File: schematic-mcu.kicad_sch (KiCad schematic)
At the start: 24 parts, among them U5 USBLC6-2P6, U6 ESP32-S3FN8, Y1 Crystal_GND24

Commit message: PCB Drawing
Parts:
- C1, C2, C28, C29, C30, C31, C32, C33, C34, C35, C4, C5, C8: footprint (none) -> Capacitor_SMD:C_1206_3216Metric
- L3: footprint (none) -> Inductor_SMD:LQG15WH0N7B02D
- R23, R5: footprint (none) -> Resistor_SMD:R_1206_3216Metric
- Y1: footprint (none) -> Crystal:KC3225K400000C1GE00
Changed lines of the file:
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@@
       (effects (font (size 1.27 1.27)) (justify left))
     )
-    (property "Footprint" "" (at 186.3852 60.96 0)
+    (property "Footprint" "Capacitor_SMD:C_1206_3216Metric" (at 186.3852 60.96 0)
       (effects (font (size 1.27 1.27)) hide)
     )
@@
       (effects (font (size 1.27 1.27)) (justify left))
     )
-    (property "Footprint" "" (at 164.7952 60.96 0)
+    (property "Footprint" "Capacitor_SMD:C_1206_3216Metric" (at 164.7952 60.96 0)
       (effects (font (size 1.27 1.27)) hide)
     )
@@
       (effects (font (size 1.27 1.27)) (justify left))
     )
-    (property "Footprint" "" (at 176.2252 60.96 0)
+    (property "Footprint" "Capacitor_SMD:C_1206_3216Metric" (at 176.2252 60.96 0)
       (effects (font (size 1.27 1.27)) hide)
     )
@@
       (effects (font (size 1.27 1.27)) (justify left))
     )
-    (property "Footprint" "" (at 213.0552 46.99 0)
+    (property "Footprint" "Capacitor_SMD:C_1206_3216Metric" (at 213.0552 46.99 0)
       (effects (font (size 1.27 1.27)) hide)
     )
@@
       (effects (font (size 1.27 1.27)) (justify left))
     )
-    (property "Footprint" "" (at 83.5152 49.53 0)
+    (property "Footprint" "Capacitor_SMD:C_1206_3216Metric" (at 83.5152 49.53 0)
       (effects (font (size 1.27 1.27)) hide)
     )
@@
       (effects (font (size 1.27 1.27)))
     )
-    (property "Footprint" "" (at 194.31 53.34 0)
+    (property "Footprint" "Inductor_SMD:LQG15WH0N7B02D" (at 194.31 53.34 0)
       (effects (font (size 1.27 1.27)) hide)
     )
@@
       (effects (font (size 1.27 1.27)) (justify left))
     )
-    (property "Footprint" "" (at 124.1552 49.53 0)
+    (property "Footprint" "Capacitor_SMD:C_1206_3216Metric" (at 124.1552 49.53 0)
       (effects (font (size 1.27 1.27)) hide)
     )
@@
       (effects (font (size 1.27 1.27)) (justify right))
     )
-    (property "Footprint" "" (at 124.968 36.83 90)
+    (property "Footprint" "Resistor_SMD:R_1206_3216Metric" (at 124.968 36.83 90)
       (effects (font (size 1.27 1.27)) hide)
     )
@@
       (effects (font (size 1.27 1.27)) hide)
     )
-    (property "Footprint" "" (at 45.72 162.56 0)
+    (property "Footprint" "Crystal:KC3225K400000C1GE00" (at 45.72 162.56 0)
       (effects (font (size 1.27 1.27)) hide)
     )
@@
       (effects (font (size 1.27 1.27)) (justify left))
     )
-    (property "Footprint" "" (at 74.6252 114.3 0)
+    (property "Footprint" "Capacitor_SMD:C_1206_3216Metric" (at 74.6252 114.3 0)
       (effects (font (size 1.27 1.27)) hide)
     )
@@
       (effects (font (size 1.27 1.27)) (justify right))
     )
-    (property "Footprint" "" (at 44.958 36.83 90)
+    (property "Footprint" "Resistor_SMD:R_1206_3216Metric" (at 44.958 36.83 90)
       (effects (font (size 1.27 1.27)) hide)
     )
@@
       (effects (font (size 1.27 1.27)) (justify left))
     )
-    (property "Footprint" "" (at 257.5052 63.5 0)
+    (property "Footprint" "Capacitor_SMD:C_1206_3216Metric" (at 257.5052 63.5 0)
       (effects (font (size 1.27 1.27)) hide)
     )
@@
       (effects (font (size 1.27 1.27)) (justify left))
     )
-    (property "Footprint" "" (at 33.9852 172.72 0)
+    (property "Footprint" "Capacitor_SMD:C_1206_3216Metric" (at 33.9852 172.72 0)
       (effects (font (size 1.27 1.27)) hide)
     )
@@
       (effects (font (size 1.27 1.27)) (justify right))
     )
-    (property "Footprint" "" (at 245.4148 63.5 0)
+    (property "Footprint" "Capacitor_SMD:C_1206_3216Metric" (at 245.4148 63.5 0)
       (effects (font (size 1.27 1.27)) hide)
     )
@@
       (effects (font (size 1.27 1.27)) (justify right))
     )
-    (property "Footprint" "" (at 84.328 36.83 90)
+    (property "Footprint" "Resistor_SMD:R_1206_3216Metric" (at 84.328 36.83 90)
       (effects (font (size 1.27 1.27)) hide)
     )
@@
       (effects (font (size 1.27 1.27)) (justify left))
     )
-    (property "Footprint" "" (at 243.5352 46.99 0)
+    (property "Footprint" "Capacitor_SMD:C_1206_3216Metric" (at 243.5352 46.99 0)
       (effects (font (size 1.27 1.27)) hide)
     )
@@
       (effects (font (size 1.27 1.27)) hide)
     )
-    (property "Value" "PWR_FLAG" (at 219.71 48.26 0)
+    (property "Value" "PWR_FLAG" (at 219.71 49.53 0)
       (effects (font (size 1.27 1.27)))
     )
@@
       (effects (font (size 1.27 1.27)) (justify left))
     )
-    (property "Footprint" "" (at 204.1652 60.96 0)
+    (property "Footprint" "Capacitor_SMD:C_1206_3216Metric" (at 204.1652 60.96 0)
       (effects (font (size 1.27 1.27)) hide)
     )
@@
       (effects (font (size 1.27 1.27)) (justify left))
     )
-    (property "Footprint" "" (at 44.1452 49.53 0)
+    (property "Footprint" "Capacitor_SMD:C_1206_3216Metric" (at 44.1452 49.53 0)
       (effects (font (size 1.27 1.27)) hide)
     )
@@
       (effects (font (size 1.27 1.27)) (justify left))
     )
-    (property "Footprint" "" (at 58.1152 172.72 0)
-      (effects (font (size 1.27 1.27)) hide)
-    )
+    (property "Footprint" "Capacitor_SMD:C_1206_3216Metric" (at 58.1152 172.72 0)
+      (effects (font (size 1.27 1.27)) hide)
+    )

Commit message: Changing footprints for capacitors C >= 10 uF
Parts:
- C32: footprint Capacitor_SMD:C_1206_3216Metric -> Capacitor_Tantalum_SMD:EEHZT1E331UP
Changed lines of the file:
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@@
       (effects (font (size 1.27 1.27)) (justify left))
     )
-    (property "Footprint" "Capacitor_SMD:C_1206_3216Metric" (at 164.7952 60.96 0)
+    (property "Footprint" "Capacitor_Tantalum_SMD:EEHZT1E331UP" (at 164.7952 60.96 0)
       (effects (font (size 1.27 1.27)) hide)
     )

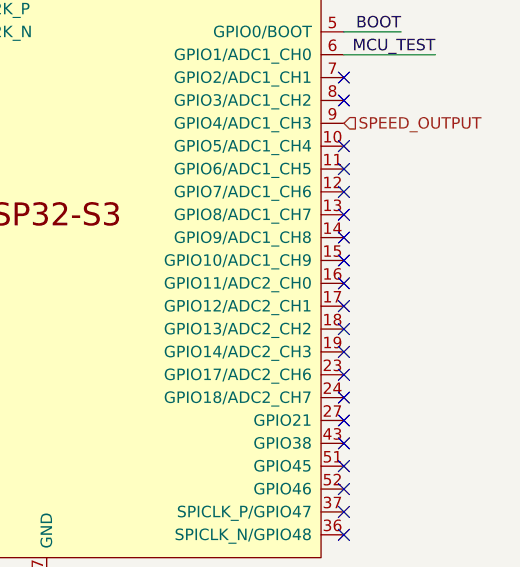
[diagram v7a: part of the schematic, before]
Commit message: Add test pins for I/O MCU
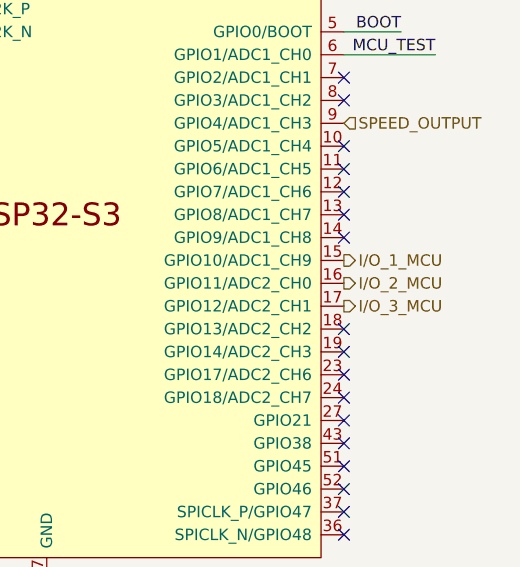
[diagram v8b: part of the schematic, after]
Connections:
- net I/O_1_MCU: now reaches U6.15 (GPIO10/ADC1_CH9)
- net I/O_2_MCU: now reaches U6.16 (GPIO11/ADC2_CH0)
- net I/O_3_MCU: now reaches U6.17 (GPIO12/ADC2_CH1)
- no-connect marks 36 -> 33
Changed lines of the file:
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@@
   (no_connect (at 195.58 128.27))
   (no_connect (at 195.58 138.43))
-  (no_connect (at 261.62 95.25))
-  (no_connect (at 261.62 118.11))
   (no_connect (at 261.62 107.95))
   (no_connect (at 261.62 113.03))
   (no_connect (at 195.58 87.63))
-  (no_connect (at 261.62 120.65))
   (no_connect (at 195.58 146.05))
   (no_connect (at 261.62 140.97))
@@
   (no_connect (at 195.58 140.97))
   (no_connect (at 261.62 74.93))
-  (no_connect (at 261.62 97.79))
   (no_connect (at 261.62 128.27))
   (no_connect (at 261.62 123.19))
   (no_connect (at 261.62 133.35))
   (no_connect (at 261.62 138.43))
-  (no_connect (at 261.62 115.57))
+  (no_connect (at 261.62 95.25))
   (no_connect (at 261.62 146.05))
   (no_connect (at 261.62 110.49))
@@
   (no_connect (at 195.58 110.49))
   (no_connect (at 261.62 135.89))
+  (no_connect (at 261.62 97.79))
   (no_connect (at 261.62 105.41))
   (wire (pts (xy 163.83 62.23) (xy 163.83 60.96))
@@
     (effects (font (size 1.27 1.27)) (justify right))
   )
+  (hierarchical_label "I{slash}O_3_MCU" (shape output) (at 261.62 120.65 0) (fields_autoplaced)
+    (effects (font (size 1.27 1.27)) (justify left))
+  )
+  (hierarchical_label "I{slash}O_1_MCU" (shape output) (at 261.62 115.57 0) (fields_autoplaced)
+    (effects (font (size 1.27 1.27)) (justify left))
+  )
   (hierarchical_label "USB_D+" (shape bidirectional) (at 40.64 105.41 180) (fields_autoplaced)
     (effects (font (size 1.27 1.27)) (justify right))
   )
+  (hierarchical_label "I{slash}O_2_MCU" (shape output) (at 261.62 118.11 0) (fields_autoplaced)
+    (effects (font (size 1.27 1.27)) (justify left))
+  )
   (symbol (lib_id "power:GND") (at 95.25 50.8 0) (unit 1)
